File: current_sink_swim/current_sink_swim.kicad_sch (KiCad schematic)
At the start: 0 parts

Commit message: add base schematic
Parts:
- added C1, C2: C, symbol Device:C
- added J2: Conn_01x02_Socket, symbol Connector:Conn_01x02_Socket
- added Q1: Q_NMOS_DGS, symbol Device:Q_NMOS_DGS
- added R1, R3: R, symbol Device:R
- added RV1: R_Potentiometer, symbol Device:R_Potentiometer
- added U1: LMV358, symbol Amplifier_Operational:LMV358
- added U2: TC1016, Package_TO_SOT_THT:TO-220-3_Vertical, symbol kody_custom_symbols:LM7805_TO220
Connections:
- new net: C2.2, J2.1 (Pin_1), Q1.1 (D), U2.1 (VI)
- new net: C1.2, RV1.2, U1.8 (V+), U2.3 (VO)
- new net: Q1.2 (G), U1.1
- new net: Q1.3 (S), R1.1, U1.2 (-)
- new net: R3.1, RV1.3, U1.3 (+)
- new net GND: C1.1, C2.1, J2.2 (Pin_2), R1.2, R3.2, U1.4 (V-), U2.2 (GND)

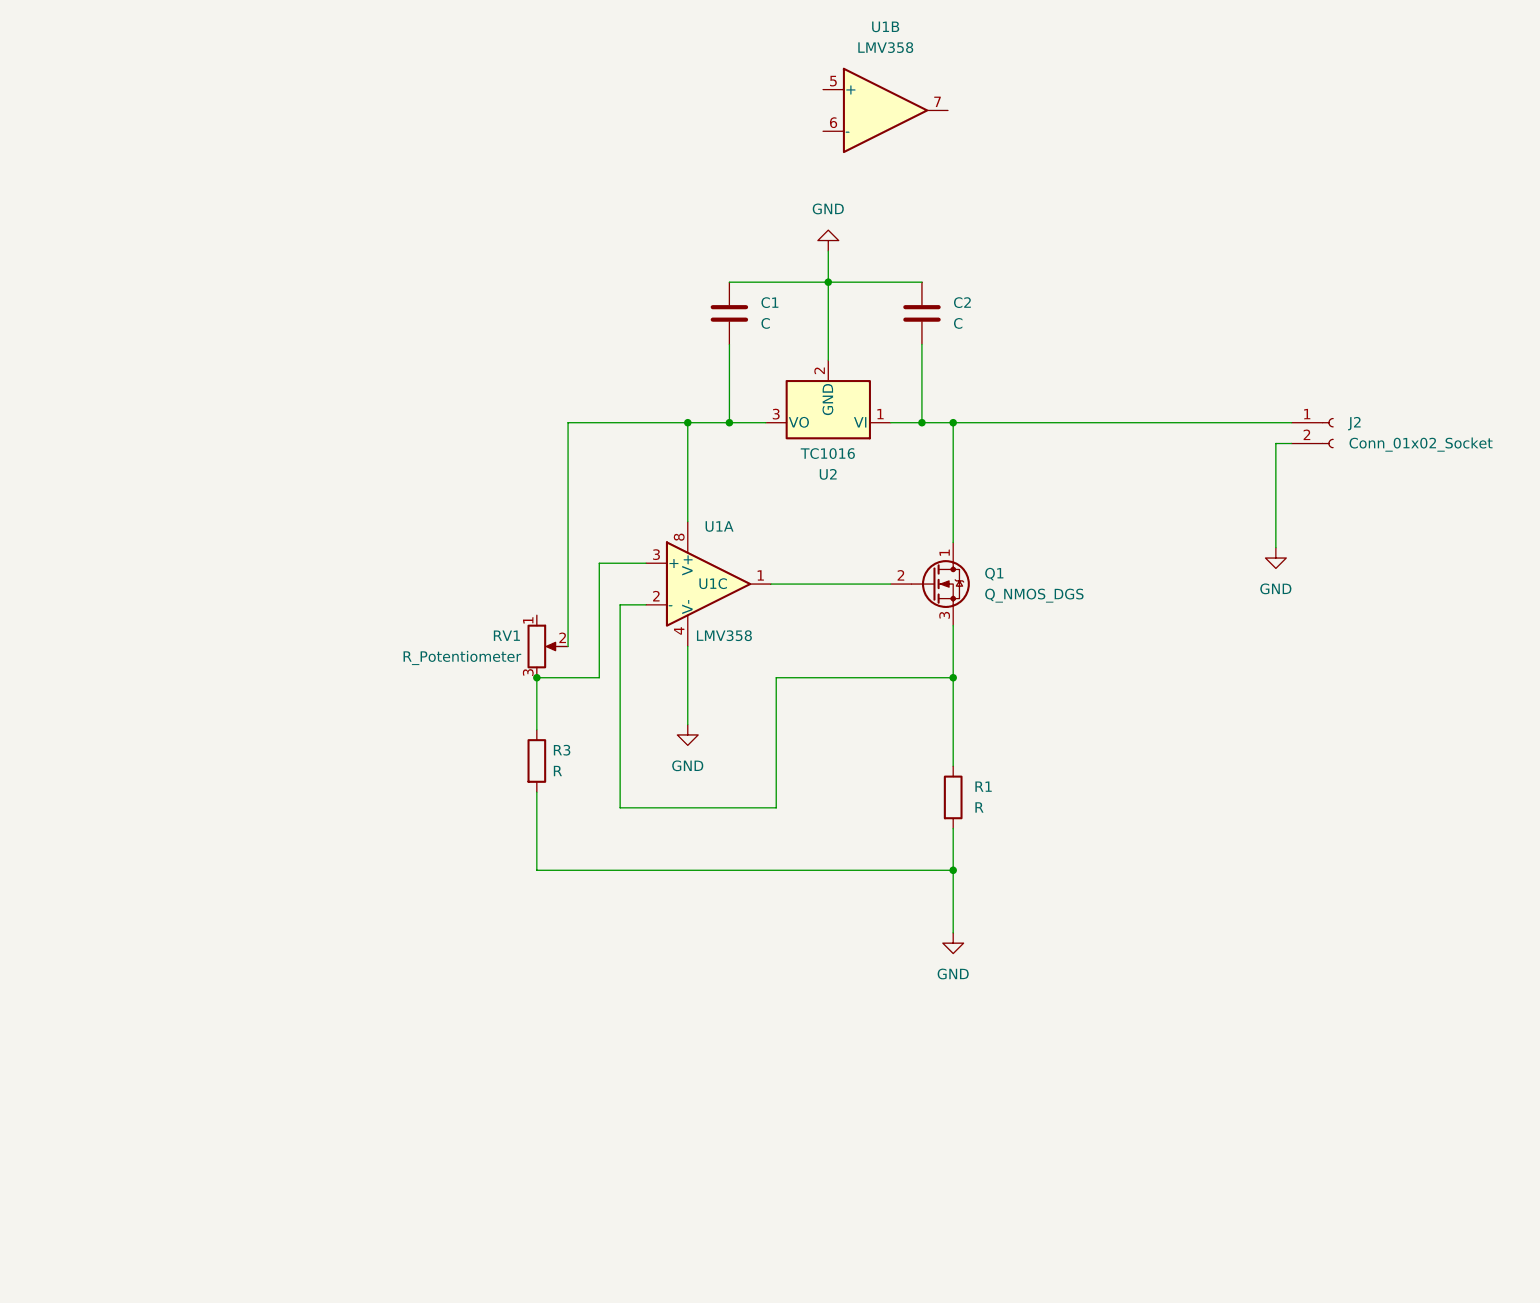
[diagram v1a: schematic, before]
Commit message: add hierarchical sheets
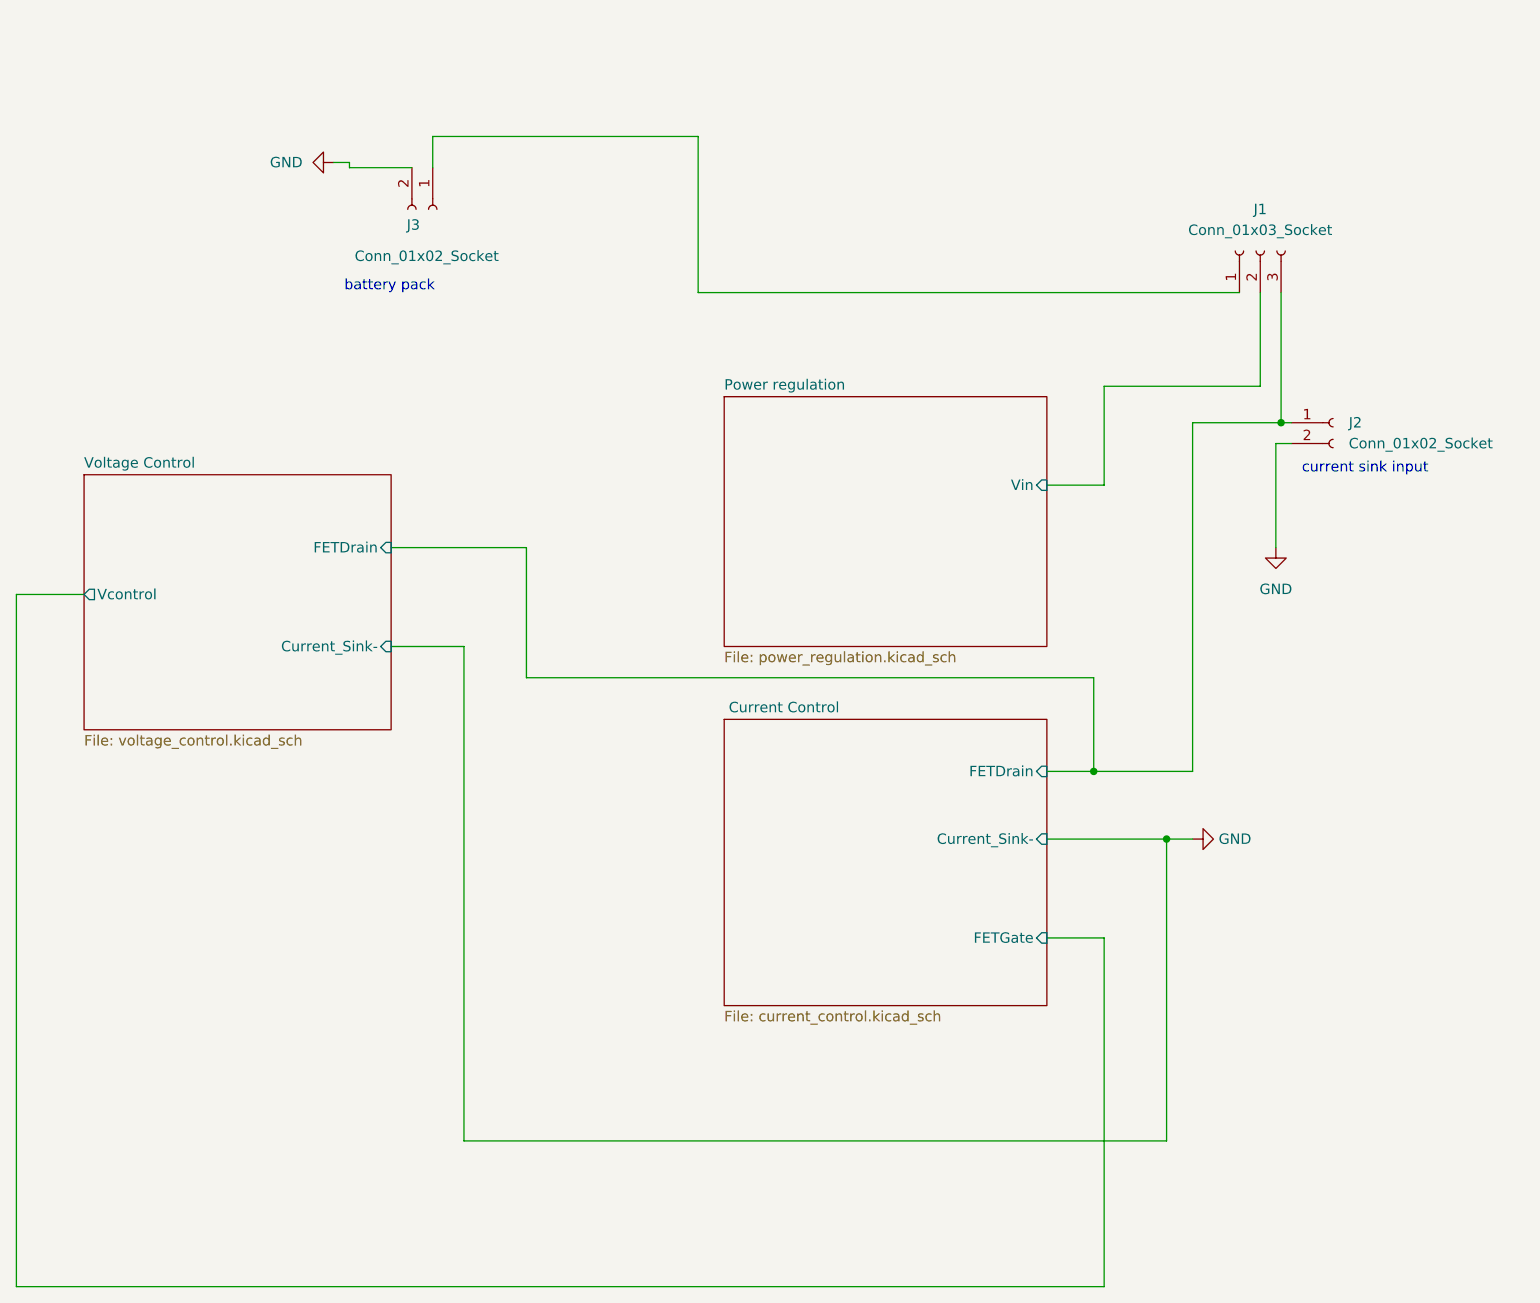
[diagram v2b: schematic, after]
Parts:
- removed C1, C2: C, symbol Device:C
- removed Q1: Q_NMOS_DGS, symbol Device:Q_NMOS_DGS
- removed R1, R3: R, symbol Device:R
- removed RV1: R_Potentiometer, symbol Device:R_Potentiometer
- removed U1: LMV358, symbol Amplifier_Operational:LMV358
- removed U2: TC1016, Package_TO_SOT_THT:TO-220-3_Vertical, symbol kody_custom_symbols:LM7805_TO220
- added J1: Conn_01x03_Socket, symbol Connector:Conn_01x03_Socket
- added J3: Conn_01x02_Socket, symbol Connector:Conn_01x02_Socket
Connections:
- net GND: now also J3.2 (Pin_2)
- net  Current Control/FETDrain: now reaches J2.1 (Pin_1)
- net  Current Control/FETDrain: now also J1.3 (Pin_3)
- new net: J1.1 (Pin_1), J3.1 (Pin_1)
- new net Power regulation/Vin: J1.2 (Pin_2)
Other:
- added sheet  Current Control (current_control.kicad_sch)
- added sheet Power regulation (power_regulation.kicad_sch)
- added sheet Voltage Control (voltage_control.kicad_sch)
- note added: "battery pack"
- note added: "current sink input"

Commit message: re-annotate schematic
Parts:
- renumbered J3 to J1, J1 to J2, J2 to J3
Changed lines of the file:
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@@
   (symbol (lib_id "power:GND") (at 55.88 31.115 270) (unit 1)
     (in_bom yes) (on_board yes) (dnp no) (fields_autoplaced)
-    (property "Reference" "#PWR06" (at 49.53 31.115 0)
+    (property "Reference" "#PWR01" (at 49.53 31.115 0)
       (effects (font (size 1.27 1.27)) hide)
     )
@@
       (project "current_sink_swim"
         (path "/d8f9bd22-1078-406d-bafe-f69bb2710c23"
-          (reference "#PWR06") (unit 1)
+          (reference "#PWR01") (unit 1)
         )
       )
@@
   (symbol (lib_id "power:GND") (at 160.655 113.665 90) (unit 1)
     (in_bom yes) (on_board yes) (dnp no) (fields_autoplaced)
-    (property "Reference" "#PWR05" (at 167.005 113.665 0)
+    (property "Reference" "#PWR02" (at 167.005 113.665 0)
       (effects (font (size 1.27 1.27)) hide)
     )
@@
       (project "current_sink_swim"
         (path "/d8f9bd22-1078-406d-bafe-f69bb2710c23"
-          (reference "#PWR05") (unit 1)
+          (reference "#PWR02") (unit 1)
         )
       )
@@
   (symbol (lib_id "power:GND") (at 170.815 78.105 0) (unit 1)
     (in_bom yes) (on_board yes) (dnp no) (fields_autoplaced)
-    (property "Reference" "#PWR04" (at 170.815 84.455 0)
+    (property "Reference" "#PWR03" (at 170.815 84.455 0)
       (effects (font (size 1.27 1.27)) hide)
     )
@@
       (project "current_sink_swim"
         (path "/d8f9bd22-1078-406d-bafe-f69bb2710c23"
-          (reference "#PWR04") (unit 1)
+          (reference "#PWR03") (unit 1)
         )
       )
@@
   (symbol (lib_id "Connector:Conn_01x03_Socket") (at 168.91 41.91 90) (unit 1)
     (in_bom yes) (on_board yes) (dnp no) (fields_autoplaced)
-    (property "Reference" "J1" (at 168.91 36.83 90)
+    (property "Reference" "J2" (at 168.91 36.83 90)
       (effects (font (size 1.27 1.27)))
     )
@@
       (project "current_sink_swim"
         (path "/d8f9bd22-1078-406d-bafe-f69bb2710c23"
-          (reference "J1") (unit 1)
+          (reference "J2") (unit 1)
         )
       )
@@
   (symbol (lib_id "Connector:Conn_01x02_Socket") (at 67.945 36.83 270) (unit 1)
     (in_bom yes) (on_board yes) (dnp no)
-    (property "Reference" "J3" (at 64.77 38.735 90)
+    (property "Reference" "J1" (at 64.77 38.735 90)
       (effects (font (size 1.27 1.27)) (justify left))
     )
@@
       (project "current_sink_swim"
         (path "/d8f9bd22-1078-406d-bafe-f69bb2710c23"
-          (reference "J3") (unit 1)
+          (reference "J1") (unit 1)
         )
       )
@@
   (symbol (lib_id "Connector:Conn_01x02_Socket") (at 177.8 62.865 0) (unit 1)
     (in_bom yes) (on_board yes) (dnp no) (fields_autoplaced)
-    (property "Reference" "J2" (at 179.705 62.865 0)
+    (property "Reference" "J3" (at 179.705 62.865 0)
       (effects (font (size 1.27 1.27)) (justify left))
     )
@@
       (project "current_sink_swim"
         (path "/d8f9bd22-1078-406d-bafe-f69bb2710c23"
-          (reference "J2") (unit 1)
+          (reference "J3") (unit 1)
         )
       )

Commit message: assign footprints and start layout
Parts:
- J1, J3: footprint (none) -> Connector_PinHeader_2.54mm:PinHeader_1x02_P2.54mm_Horizontal
- J2: footprint (none) -> Connector_PinHeader_2.54mm:PinHeader_1x03_P2.54mm_Horizontal
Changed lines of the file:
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@@
       (effects (font (size 1.27 1.27)))
     )
-    (property "Footprint" "" (at 168.91 41.91 0)
+    (property "Footprint" "Connector_PinHeader_2.54mm:PinHeader_1x03_P2.54mm_Horizontal" (at 168.91 41.91 0)
       (effects (font (size 1.27 1.27)) hide)
     )
@@
       (effects (font (size 1.27 1.27)) (justify left))
     )
-    (property "Footprint" "" (at 67.945 36.83 0)
+    (property "Footprint" "Connector_PinHeader_2.54mm:PinHeader_1x02_P2.54mm_Horizontal" (at 67.945 36.83 0)
       (effects (font (size 1.27 1.27)) hide)
     )
@@
       (effects (font (size 1.27 1.27)) (justify left))
     )
-    (property "Footprint" "" (at 177.8 62.865 0)
+    (property "Footprint" "Connector_PinHeader_2.54mm:PinHeader_1x02_P2.54mm_Horizontal" (at 177.8 62.865 0)
       (effects (font (size 1.27 1.27)) hide)
     )

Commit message: add correct pot symbols
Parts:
- J1, J3: footprint Connector_PinHeader_2.54mm:PinHeader_1x02_P2.54mm_Horizontal -> custom_modules:te_2.54_2_pin_connector
- J2: footprint Connector_PinHeader_2.54mm:PinHeader_1x03_P2.54mm_Horizontal -> custom_modules:te_2.54mm_3_pin
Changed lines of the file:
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@@
       (effects (font (size 1.27 1.27)))
     )
-    (property "Footprint" "Connector_PinHeader_2.54mm:PinHeader_1x03_P2.54mm_Horizontal" (at 168.91 41.91 0)
+    (property "Footprint" "custom_modules:te_2.54mm_3_pin" (at 168.91 41.91 0)
       (effects (font (size 1.27 1.27)) hide)
     )
@@
       (effects (font (size 1.27 1.27)) (justify left))
     )
-    (property "Footprint" "Connector_PinHeader_2.54mm:PinHeader_1x02_P2.54mm_Horizontal" (at 67.945 36.83 0)
+    (property "Footprint" "custom_modules:te_2.54_2_pin_connector" (at 67.945 36.83 0)
       (effects (font (size 1.27 1.27)) hide)
     )
@@
       (effects (font (size 1.27 1.27)) (justify left))
     )
-    (property "Footprint" "Connector_PinHeader_2.54mm:PinHeader_1x02_P2.54mm_Horizontal" (at 177.8 62.865 0)
+    (property "Footprint" "custom_modules:te_2.54_2_pin_connector" (at 177.8 62.865 0)
       (effects (font (size 1.27 1.27)) hide)
     )

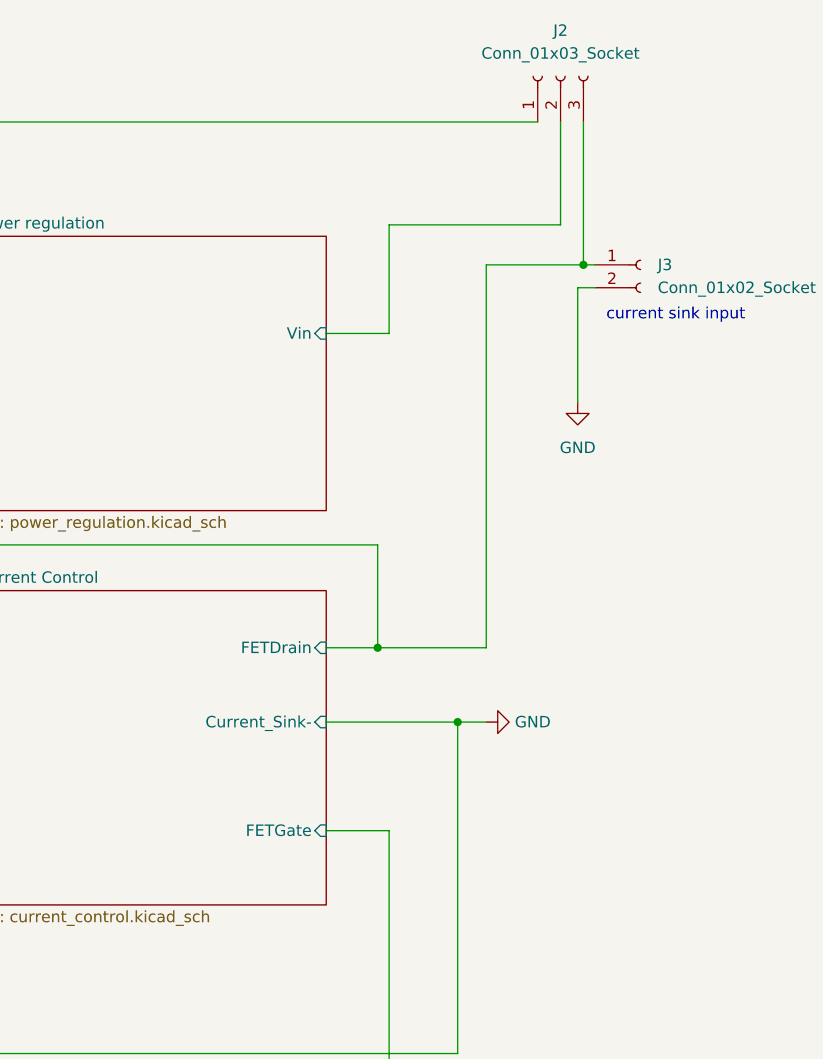
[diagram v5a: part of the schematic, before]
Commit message: first attempt at layout. Probably will be ripped up
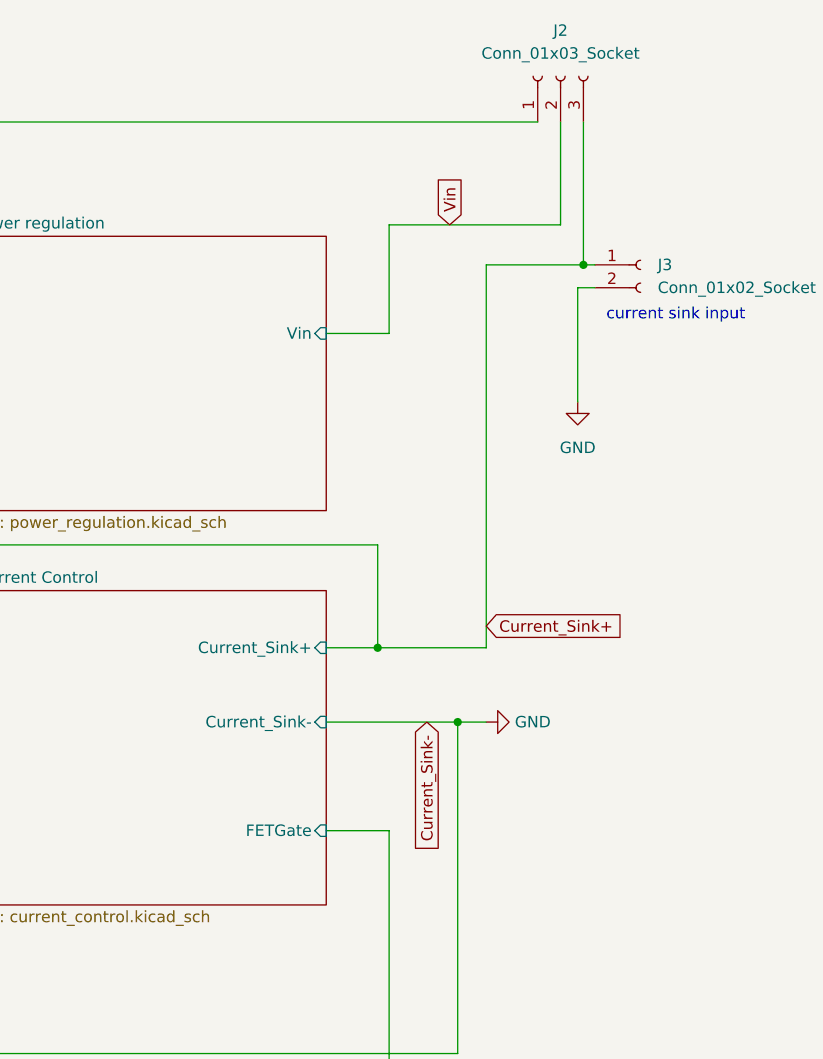
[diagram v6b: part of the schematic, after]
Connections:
- net  Current Control/FETDrain renamed Current_Sink+
- net Power regulation/Vin renamed Vin
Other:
- sheet  Current Control ports: added Current_Sink+; removed FETDrain
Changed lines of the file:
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@@
     (effects (font (size 1.27 1.27)) (justify left bottom))
+  )
+  (global_label "Vin" (shape input) (at 156.591 58.42 90) (fields_autoplaced)
+    (effects (font (size 1.27 1.27)) (justify left))
+    (property "Intersheetrefs" "${INTERSHEET_REFS}" (at 156.591 52.5924 90)
+      (effects (font (size 1.27 1.27)) (justify left) hide)
+    )
+  )
+  (global_label "Current_Sink-" (shape input) (at 154.051 113.665 270) (fields_autoplaced)
+    (effects (font (size 1.27 1.27)) (justify right))
+    (property "Intersheetrefs" "${INTERSHEET_REFS}" (at 154.051 130.1363 90)
+      (effects (font (size 1.27 1.27)) (justify right) hide)
+    )
+  )
+  (global_label "Current_Sink+" (shape input) (at 160.655 102.997 0) (fields_autoplaced)
+    (effects (font (size 1.27 1.27)) (justify left))
+    (property "Intersheetrefs" "${INTERSHEET_REFS}" (at 177.1263 102.997 0)
+      (effects (font (size 1.27 1.27)) (justify left) hide)
+    )
   )
   (symbol (lib_id "power:GND") (at 55.88 31.115 270) (unit 1)
@@
       (effects (font (size 1.27 1.27)) (justify left top))
     )
-    (pin "FETDrain" input (at 142.875 105.41 0)
-      (effects (font (size 1.27 1.27)) (justify right))
-    )
     (pin "FETGate" input (at 142.875 125.73 0)
       (effects (font (size 1.27 1.27)) (justify right))
@@
       (effects (font (size 1.27 1.27)) (justify right))
     )
+    (pin "Current_Sink+" input (at 142.875 105.41 0)
+      (effects (font (size 1.27 1.27)) (justify right))
+    )

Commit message: initial generation of gerber files
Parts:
- J1: MPN (none) -> 282834-2
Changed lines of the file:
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@@
+      (effects (font (size 1.27 1.27)) hide)
+    )
+    (property "MPN" "282834-2" (at 67.945 36.83 0)
       (effects (font (size 1.27 1.27)) hide)
     )
